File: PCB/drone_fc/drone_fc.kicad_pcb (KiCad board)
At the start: 2 copper layers, 35.1 x 37.6 mm, 45 parts, among them J1 USB_C_Receptacle_USB2.0_16P, J2 Conn_01x04_Socket, J3 Conn_01x08_Socket, SW1 PTS820J25M, U1 nRF52840, U2 USBLC6-2SC6, U3 ICM-20948, U4 MCP1703AT-3302E/DB, U5 LP5907MFX-1.8, U6 TCA9517A, X1 32MHz

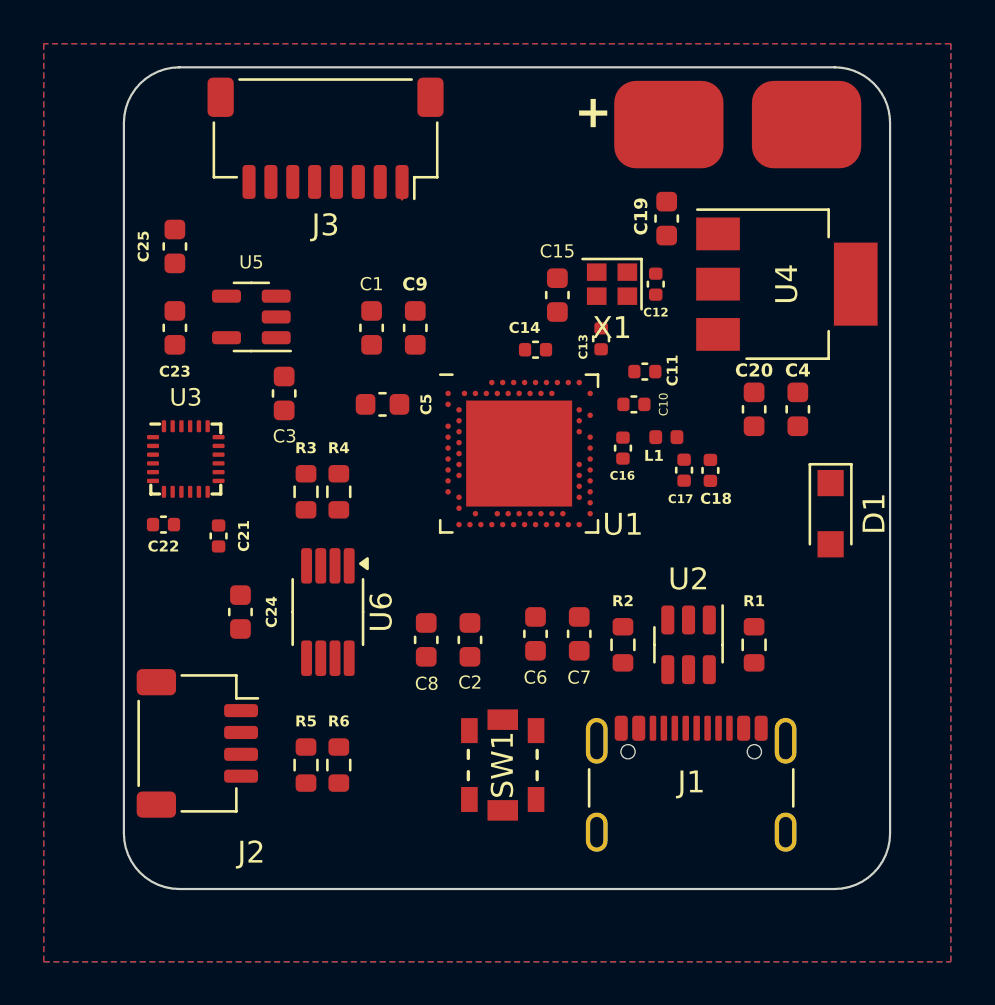
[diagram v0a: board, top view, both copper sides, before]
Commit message: Changed reset button, still need a header for SWD, and decided to move to a 4-layer board just to add some difficulty
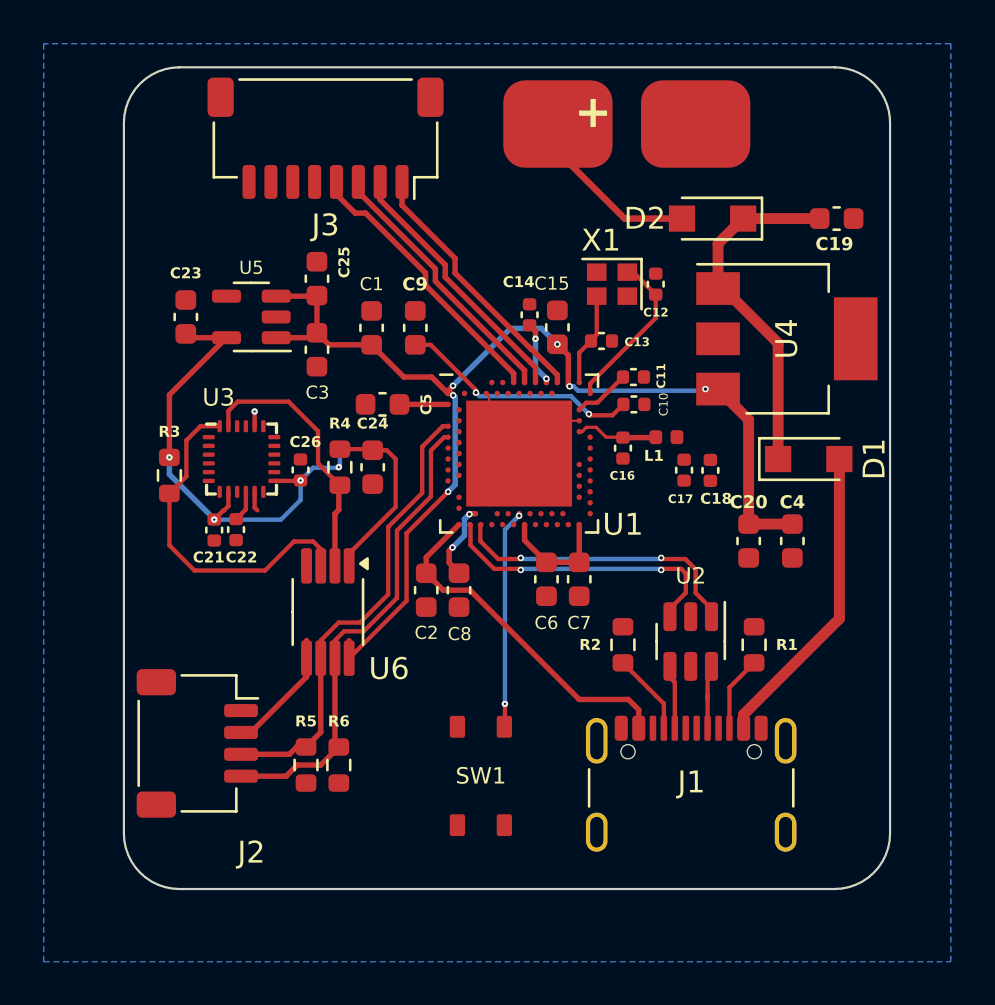
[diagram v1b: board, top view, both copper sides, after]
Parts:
- added C26: 0u1, Capacitor_SMD:C_0402_1005Metric, F.Cu at (101.8, 67.5)
- added D2: D_Schottky, Diode_SMD:Nexperia_CFP3_SOD-123W, F.Cu at (120.6, 56.0)
- C15: value 1u -> 100n
- SW1: value PTS820J25M -> PTS815SJM250SMTRLFS; footprint footprints:SW2_PTS820J25MSMTRLFS_CNK -> footprints:PTS815SJM250SMTRLFS
- moved C24 8.97 mm to (105.0, 67.4)
- moved C19 7.78 mm to (126.3, 56.0), turned to 0 degrees
- moved C25 6.67 mm to (102.5, 58.8)
- moved R3 6.29 mm to (95.8, 67.8), turned to -90 degrees
- moved C20 6.03 mm to (122.2, 70.8)
- moved C4 6.03 mm to (124.2, 70.8)
- moved BT1 5.08 mm to (116.7, 54.9)
- moved C22 3.33 mm to (98.8, 70.2), turned to -90 degrees
- moved C2 3.03 mm to (107.5, 73.0)
- moved C8 2.73 mm to (109.0, 73.0)
- moved D1 2.69 mm to (125.0, 67.0), turned to 0 degrees
- moved U3 2.55 mm to (99.0, 67.0)
- moved C6 2.55 mm to (113.0, 72.5)
- moved C3 2.50 mm to (102.5, 62.0)
- moved C7 2.50 mm to (114.5, 72.5)
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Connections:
- C19 pad 1: +15V -> Net-(D1-K)
- D1 pad 1: +15V -> Net-(D1-K)
- SW1 pad 2: GND -> (no net)
- SW1 pad 4: (no net) -> GND
- U2 pad 1: /D- -> /D+
- U2 pad 3: /D+ -> /D-
- U2 pad 4: /DR+ -> /DR-
- U2 pad 6: /DR- -> /DR+
- U4 pad 1: +15V -> Net-(D1-K)
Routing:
- net 3V3: track 0.00 -> 63.3 mm, vias 0 -> 6
- net +1V8: track 0.00 -> 31.5 mm, vias 0 -> 4
- net VBUS: track 0.00 -> 30.1 mm
- net /SCL: track 0.00 -> 22.0 mm
- net /SDA: track 0.00 -> 21.2 mm
- net Net-(D1-K): track 0.00 -> 16.3 mm
- net Net-(U3-SDA/SDI): track 0.00 -> 15.8 mm
- net /D-: track 0.00 -> 13.7 mm, vias 0 -> 2
- net /D+: track 0.00 -> 13.7 mm, vias 0 -> 2
- net /M4: track 0.00 -> 12.8 mm
- net /M3: track 0.00 -> 12.3 mm
- net Net-(U3-SCL/SCLK): track 0.00 -> 12.2 mm
- net /M2: track 0.00 -> 12.1 mm
- net /M1: track 0.79 -> 12.1 mm
- net /DEC4_6: track 0.00 -> 11.2 mm, vias 0 -> 2
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- added copper zone on In1.Cu, net GND
- removed copper zone on F.Cu, net GND
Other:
- copper layers 2 -> 4

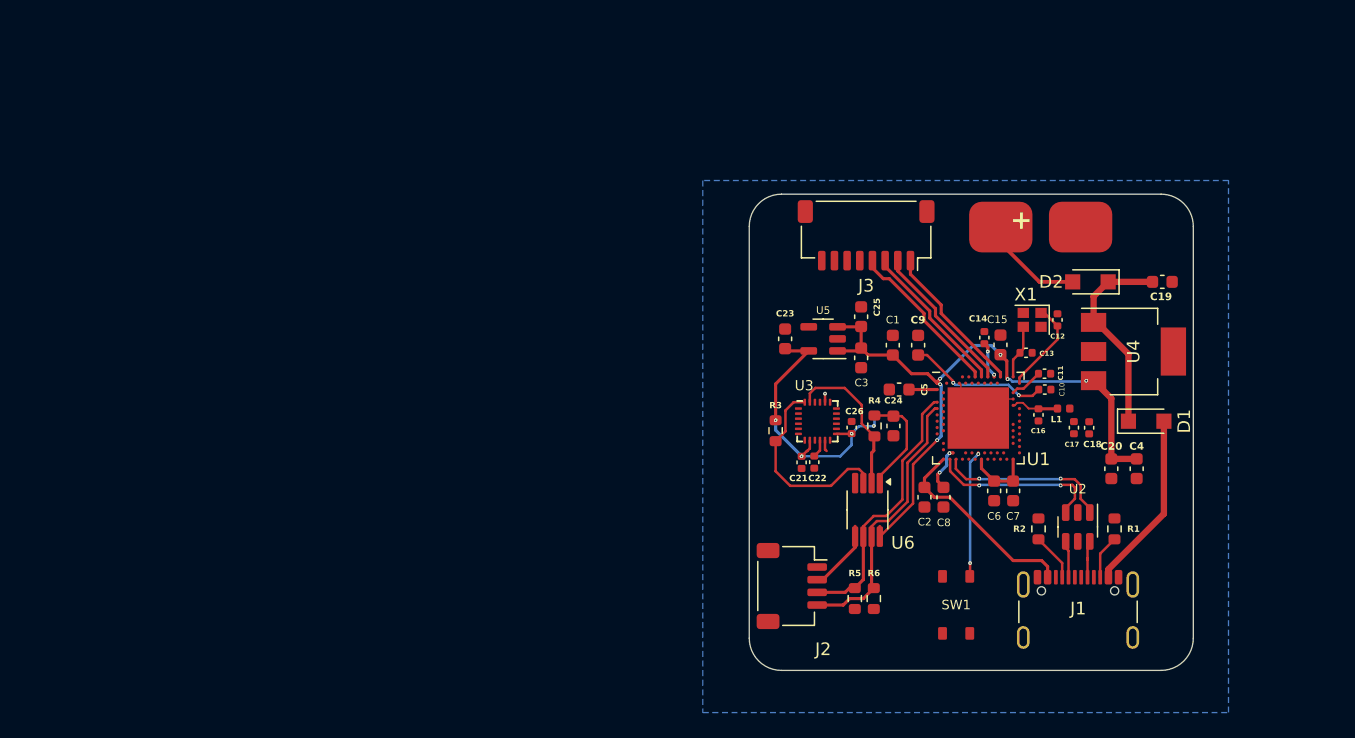
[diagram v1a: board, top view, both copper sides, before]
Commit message: Stepping back from PCB to ensure the schematic is actually done and to read up on better PCB design. Will likely start from scratch. Did add mounting holes since I completely forgot that earlier
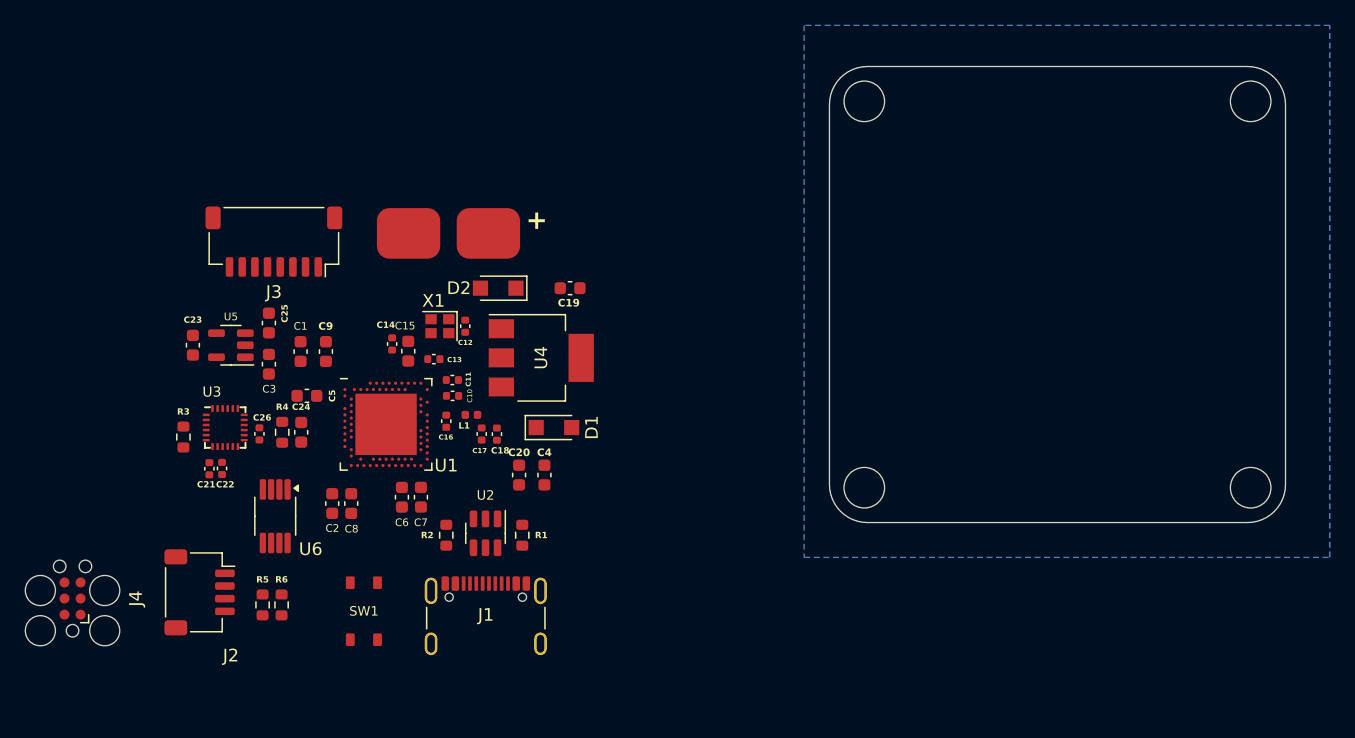
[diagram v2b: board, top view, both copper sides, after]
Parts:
- added J4: Conn_ARM_SWD_TagConnect_TC2030, Connector:Tag-Connect_TC2030-IDC-FP_2x03_P1.27mm_Vertical, F.Cu at (40.2, 81.0)
- added REF**1: MountingHole_3.2mm_M3, MountingHole:MountingHole_3.2mm_M3, F.Cu at (133.2, 72.2)
- added REF**2: MountingHole_3.2mm_M3, MountingHole:MountingHole_3.2mm_M3, F.Cu at (102.8, 41.8)
- added REF**3: MountingHole_3.2mm_M3, MountingHole:MountingHole_3.2mm_M3, F.Cu at (133.2, 41.8)
- added REF**4: MountingHole_3.2mm_M3, MountingHole:MountingHole_3.2mm_M3, F.Cu at (102.8, 72.2)
- moved J2 46.8 mm to (50.3, 80.5)
- moved J3 46.8 mm to (56.1, 52.8)
- moved BT1 46.8 mm to (70.0, 55.4)
- moved C1 46.8 mm to (58.2, 61.5)
- moved C10 46.8 mm to (70.2, 65.0)
- moved C11 46.8 mm to (70.2, 63.8)
- moved C12 46.8 mm to (71.2, 59.5)
- moved C13 46.8 mm to (68.8, 62.1)
- moved C14 46.8 mm to (65.5, 60.9)
- moved C15 46.8 mm to (66.8, 61.5)
- moved C16 46.8 mm to (69.8, 67.0)
- moved C17 46.8 mm to (72.5, 68.0)
- moved C18 46.8 mm to (73.8, 68.0)
- moved C19 46.8 mm to (79.5, 56.5)
- moved C2 46.8 mm to (60.8, 73.5)
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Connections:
- U1 pad AD22: unconnected-(U1-TRACEDATA0/P1.00-PadAD22) -> /SWO
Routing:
- net 3V3: track 63.3 -> 0.00 mm, vias 6 -> 0
- net +1V8: track 31.5 -> 0.00 mm, vias 4 -> 0
- net VBUS: track 30.1 -> 0.00 mm
- net /SCL: track 22.0 -> 0.00 mm
- net /SDA: track 21.2 -> 0.00 mm
- net Net-(D1-K): track 16.3 -> 0.00 mm
- net Net-(U3-SDA/SDI): track 15.8 -> 0.00 mm
- net /D-: track 13.7 -> 0.00 mm, vias 2 -> 0
- net /D+: track 13.7 -> 0.00 mm, vias 2 -> 0
- net /M4: track 12.8 -> 0.00 mm
- net /M3: track 12.3 -> 0.00 mm
- net Net-(U3-SCL/SCLK): track 12.2 -> 0.00 mm
- net /M1: track 12.1 -> 0.00 mm
- net /M2: track 12.1 -> 0.00 mm
- net /DEC4_6: track 11.2 -> 0.00 mm, vias 2 -> 0
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- removed copper zone on In1.Cu, net GND
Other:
- board size 35.1 x 37.6 mm -> 36 x 36 mm

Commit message: It's... done? I still have to create and route the VL53L4CX interrupt signal but otherwise I think this just needs some more grounding. I made sure that vias weren't on top of unrelated traces just in case JLCPCB doesn't support blind vias on their basic PCBs, but if they don't then I'm not sure what I'm going to do about the NRESET pin or the large die pad. I might have to contact them.
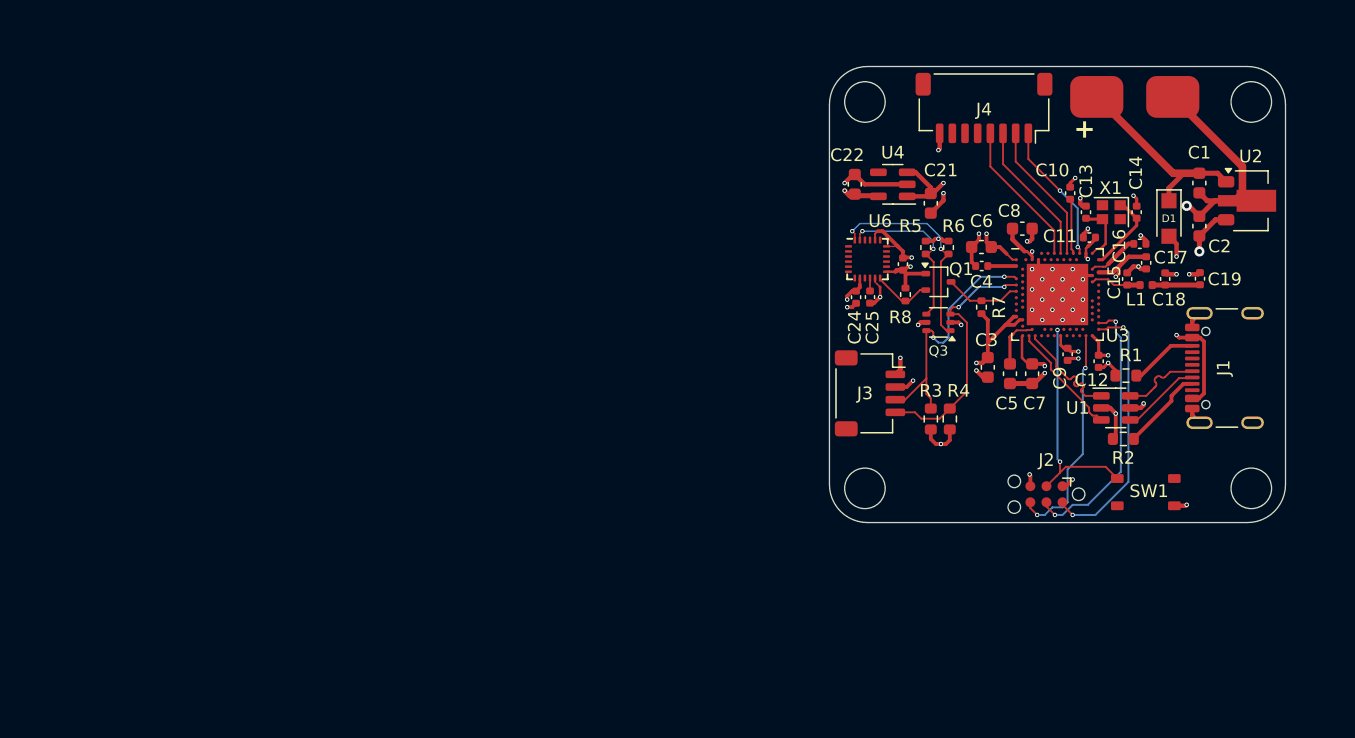
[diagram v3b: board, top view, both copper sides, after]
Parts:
- removed the C24 at (58.3, 67.9)
- removed the C25 at (55.8, 59.2)
- removed D2: D_Schottky, Diode_SMD:Nexperia_CFP3_SOD-123W
- removed REF**4: MountingHole_3.2mm_M3, MountingHole:MountingHole_3.2mm_M3
- removed the U6 at (56.2, 74.5)
- added Q1: BSS138, Package_TO_SOT_SMD:SOT-323_SC-70, F.Cu at (108.6, 56.0)
- added Q3: BSS138BKS, Package_TO_SOT_SMD:SOT-363_SC-70-6, F.Cu at (108.6, 59.2)
- added R7: 4k7, Resistor_SMD:R_0402_1005Metric, F.Cu at (112.0, 58.0)
- added R8: 4k7, Resistor_SMD:R_0402_1005Metric, F.Cu at (106.0, 57.0)
- added REF**: MountingHole_3.2mm_M3, MountingHole:MountingHole_3.2mm_M3, F.Cu at (133.3, 72.3)
- C11: renamed from C15; footprint Capacitor_SMD:C_0603_1608Metric -> Capacitor_SMD:C_0402_1005Metric
- C12: renamed from C7; footprint Capacitor_SMD:C_0603_1608Metric -> Capacitor_SMD:C_0402_1005Metric
- C4: renamed from C5; footprint Capacitor_SMD:C_0603_1608Metric -> Capacitor_SMD:C_0402_1005Metric
- C9: renamed from C6; footprint Capacitor_SMD:C_0603_1608Metric -> Capacitor_SMD:C_0402_1005Metric
- J2: renamed from J4; footprint Connector:Tag-Connect_TC2030-IDC-FP_2x03_P1.27mm_Vertical -> Connector:Tag-Connect_TC2030-IDC-NL_2x03_P1.27mm_Vertical
- R5: renamed from R3; footprint Resistor_SMD:R_0603_1608Metric -> Resistor_SMD:R_0402_1005Metric
- R6: renamed from R4; footprint Resistor_SMD:R_0603_1608Metric -> Resistor_SMD:R_0402_1005Metric
- U2: renamed from U4; value MCP1703AT-3302E/DB -> MCP1703AT-3302E/MB; footprint Package_TO_SOT_SMD:SOT-223-3_TabPin2 -> Package_TO_SOT_SMD:SOT-89-3
- moved J2 77.3 mm to (117.1, 72.8), turned to 180 degrees
- moved J1 62.9 mm to (132.3, 62.8), turned to 90 degrees
- moved R5 60.5 mm to (107.6, 53.3)
- moved SW1 59.0 mm to (122.7, 71.5), turned to 0 degrees
- moved U2 57.4 mm to (133.3, 49.6)
- moved C2 57.2 mm to (129.2, 51.6), turned to 90 degrees
- moved C26 57.1 mm to (105.8, 54.6), turned to 90 degrees
- moved J4 57.0 mm to (112.2, 42.3)
- moved C19 56.8 mm to (129.2, 55.8), turned to -90 degrees
- moved C7 56.2 mm to (116.0, 63.2)
- moved C8 55.8 mm to (115.2, 51.8), turned to 0 degrees
- moved C17 55.7 mm to (125.0, 54.5), turned to -90 degrees
- moved BT1 55.4 mm to (124.1, 43.4)
- moved C16 55.3 mm to (124.5, 53.0)
- moved C18 55.3 mm to (126.5, 55.8), turned to -90 degrees
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- renumbered C19 to C1, C14 to C10, C12 to C14, C16 to C15, C11 to C16, C10 to C17, C17 to C18, C18 to C19, C20 to C2, C3 to C21, C23 to C22, C26 to C24, C22 to C25, C21 to C26, C4 to C3, C8 to C5, C1 to C6, C2 to C7, C9 to C8, J2 to J3, J3 to J4, R5 to R3, R6 to R4, U2 to U1, U1 to U3, U5 to U4, U3 to U6
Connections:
- C1 pad 1: Net-(D1-K) -> +15V
- D1 pad 1: Net-(D1-K) -> +15V
- R3 pad 1: VDD -> 3V3
- R4 pad 1: VDD -> 3V3
- R5 pad 2: Net-(U3-SDA/SDI) -> /SCL_1_8
- R6 pad 2: Net-(U3-SCL/SCLK) -> /SDA_1_8
- SW1 pad 1: Net-(U1-P0.18/~{RESET}) -> /NRESET
- U2 pad 1: Net-(D1-K) -> +15V
- U3 pad A10: /VBAT -> unconnected-(U3-AIN5/P0.29-PadA10)
- U3 pad AC13: Net-(U1-P0.18/~{RESET}) -> /NRESET
- U3 pad L1: unconnected-(U1-P0.06-PadL1) -> /IMU_INT
- U6 pad 23: Net-(U3-SCL/SCLK) -> /SCL_1_8
- U6 pad 24: Net-(U3-SDA/SDI) -> /SDA_1_8
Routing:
- net GND: track 0.00 -> 67.9 mm, vias 0 -> 43
- net 3V3: track 0.00 -> 37.3 mm, vias 0 -> 11
- net VBUS: track 0.00 -> 31.6 mm, vias 0 -> 3
- net /SWDCLK: track 0.00 -> 21.4 mm, vias 0 -> 2
- net /SWDIO: track 0.00 -> 21.2 mm, vias 0 -> 2
- net /SDA: track 0.00 -> 20.7 mm, vias 0 -> 2
- net /SCL: track 0.00 -> 20.1 mm, vias 0 -> 2
- net /NRESET: track 0.00 -> 18.0 mm, vias 0 -> 2
- net /SWO: track 0.00 -> 17.8 mm, vias 0 -> 2
- net +15V: track 0.00 -> 16.9 mm
- net /SDA_1_8: track 0.00 -> 16.7 mm, vias 0 -> 2
- net /DEC4_6: track 0.00 -> 16.6 mm, vias 0 -> 2
- net +1V8: track 0.00 -> 13.6 mm, vias 0 -> 6
- net /SCL_1_8: track 0.00 -> 13.3 mm, vias 0 -> 2
- net /M4: track 0.00 -> 11.6 mm
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- added copper zone on In2.Cu, net +1V8
- added copper zone on In2.Cu, net 3V3
- added copper zone on In1.Cu, net GND
- removed copper zone on B.Cu, net GND
